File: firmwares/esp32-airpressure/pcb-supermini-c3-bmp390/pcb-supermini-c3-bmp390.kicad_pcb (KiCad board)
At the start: 2 copper layers, 43.8 x 70.8 mm, 11 parts, among them J1 JST GH 4_Socket, U1 ESP32-C3_SUPERMINI_SMD, U2 BMP390 MODULE, U3 CAN transciever

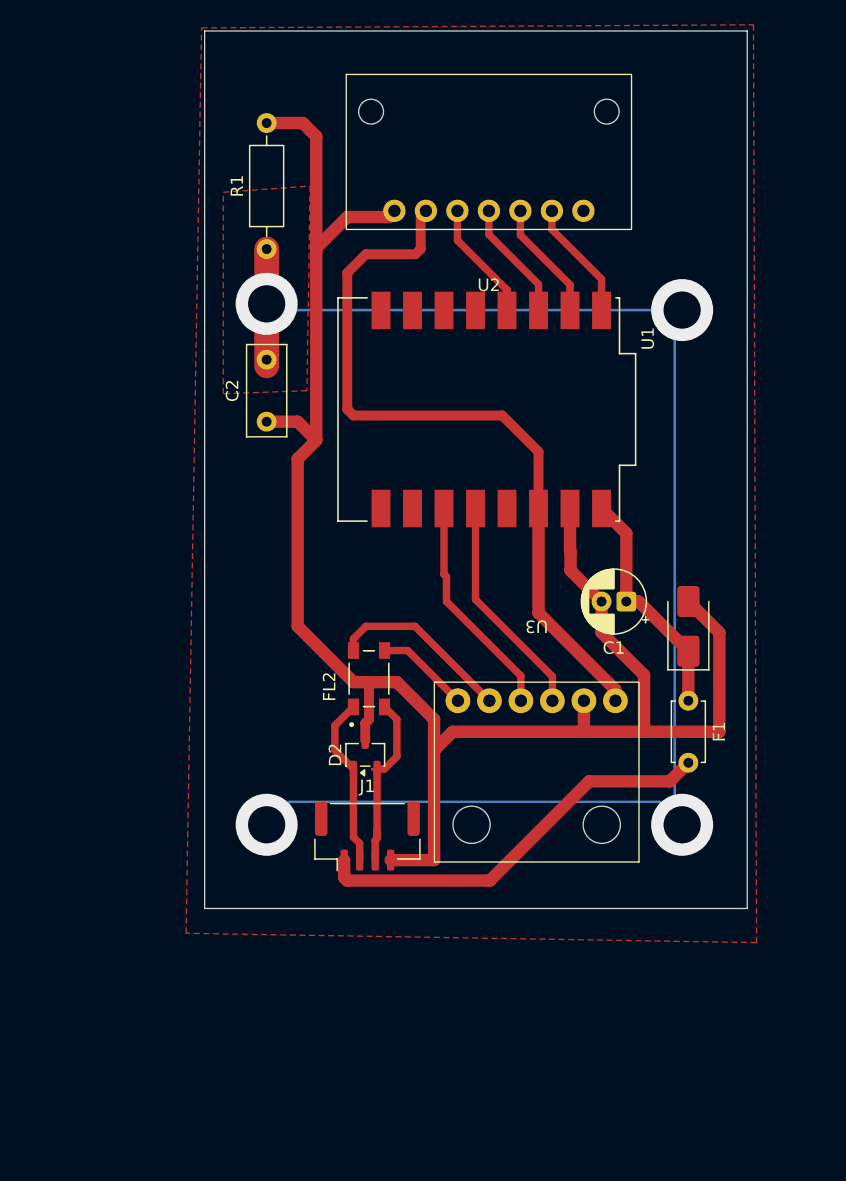
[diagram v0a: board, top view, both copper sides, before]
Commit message: refactor: update PCB to be on 2 layers
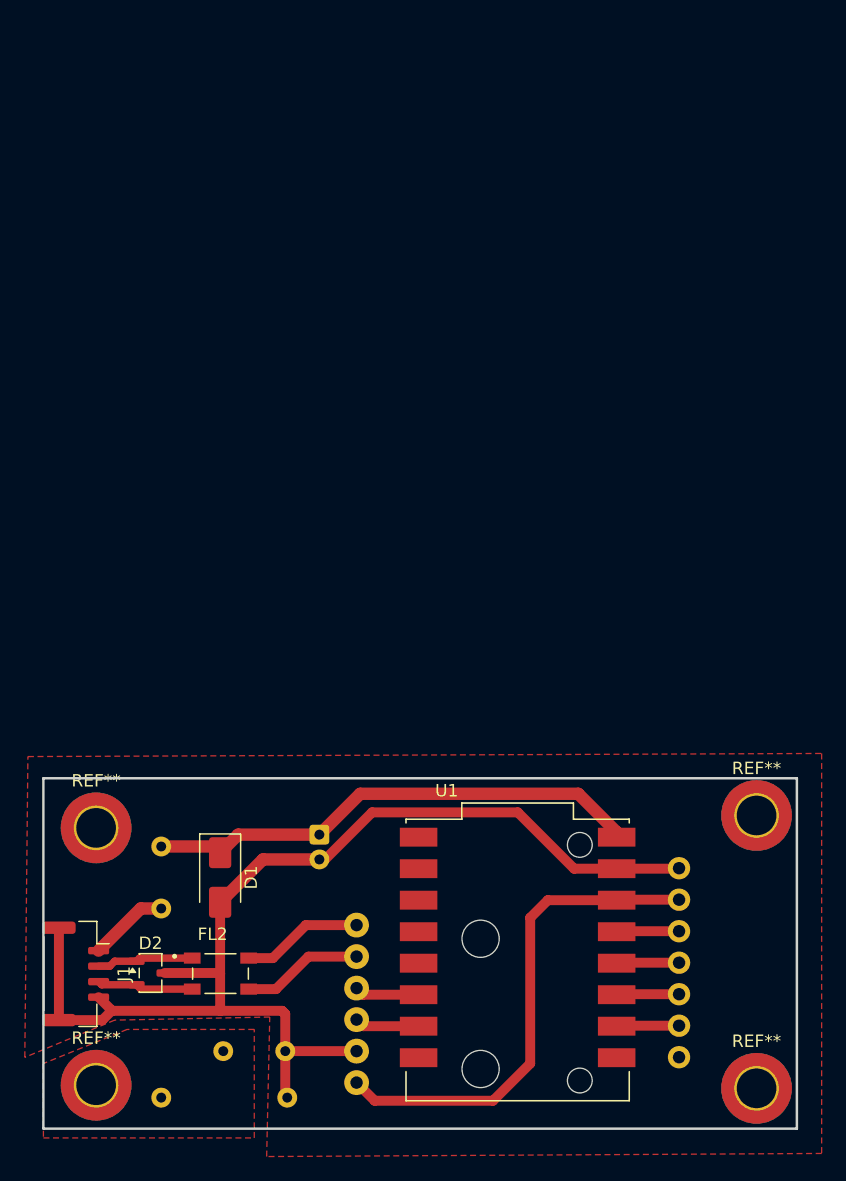
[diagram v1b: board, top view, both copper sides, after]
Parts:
- added REF**: MountingHole_3.2mm_M3_ISO7380_Pad_TopBottom, MountingHole:MountingHole_3.2mm_M3_ISO7380_Pad_TopBottom, F.Cu at (138.0, 141.2)
- added REF**: MountingHole_3.2mm_M3_ISO7380_Pad_TopBottom, MountingHole:MountingHole_3.2mm_M3_ISO7380_Pad_TopBottom, F.Cu at (84.8, 141.0)
- added REF**: MountingHole_3.2mm_M3_ISO7380_Pad_TopBottom, MountingHole:MountingHole_3.2mm_M3_ISO7380_Pad_TopBottom, F.Cu at (84.8, 120.2)
- added REF**: MountingHole_3.2mm_M3_ISO7380_Pad_TopBottom, MountingHole:MountingHole_3.2mm_M3_ISO7380_Pad_TopBottom, F.Cu at (138.0, 119.2)
- C1, C2, F1, R1, U2, U3: moved to B.Cu
- J1: footprint Connector_JST:JST_GH_BM04B-GHS-TBT_1x04-1MP_P1.25mm_Vertical -> Connector_JST:JST_GH_SM04B-GHS-TB_1x04-1MP_P1.25mm_Horizontal
- moved R1 68.9 mm to (90.0, 142.0), turned to 0 degrees
- moved U2 61.5 mm to (133.2, 131.1), turned to -90 degrees
- moved C2 50.8 mm to (100.0, 138.2), turned to 180 degrees
- moved U1 44.5 mm to (118.7, 130.9), turned to 0 degrees
- moved F1 44.1 mm to (90.0, 121.8)
- moved D1 42.8 mm to (94.8, 124.2), turned to -90 degrees
- moved C1 31.1 mm to (102.8, 120.8), turned to -90 degrees
- moved U3 30.5 mm to (104.2, 134.4), turned to 90 degrees
- moved FL2 26.6 mm to (94.8, 132.0), turned to 0 degrees
- moved J1 26.0 mm to (83.1, 132.0), turned to -90 degrees
- moved D2 24.7 mm to (89.1, 131.9), turned to 0 degrees
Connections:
- net GND renamed GND-EMS
- FL2 pad 3: Net-(U3-CANL) -> Net-(U3-CANH)
- FL2 pad 4: Net-(U3-CANH) -> Net-(U3-CANL)
- U1 pad 1: unconnected-(U1-GPIO1-Pad1) -> Net-(U1-GPIO1)
- U1 pad 10: unconnected-(U1-GPIO10-Pad10) -> Net-(U1-GPIO10)
- U1 pad 20: unconnected-(U1-GPIO20-Pad20) -> Net-(U1-GPIO20)
- U1 pad 4: unconnected-(U1-GPIO4-Pad4) -> Net-(U1-GPIO4)
- U1 pad 5: Net-(U1-GPIO5) -> unconnected-(U1-GPIO5-Pad5)
- U1 pad 6: Net-(U1-GPIO6) -> unconnected-(U1-GPIO6-Pad6)
- U1 pad 7: Net-(U1-GPIO7) -> unconnected-(U1-GPIO7-Pad7)
- U1 pad 8: Net-(U1-GPIO8) -> unconnected-(U1-GPIO8-Pad8)
- U2 pad 3: Net-(U1-GPIO8) -> Net-(U1-GPIO4)
- U2 pad 4: Net-(U1-GPIO7) -> Net-(U1-GPIO3)
- U2 pad 5: Net-(U1-GPIO6) -> Net-(U1-GPIO2)
- U2 pad 6: Net-(U1-GPIO5) -> Net-(U1-GPIO1)
- U3 pad 3: Net-(U1-GPIO3) -> Net-(U1-GPIO20)
- U3 pad 4: Net-(U1-GPIO2) -> Net-(U1-GPIO10)
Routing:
- net GND-EMS: track 120.2 -> 0.00 mm, vias 4 -> 0
- net GNDREF: track 148.8 -> 95.4 mm
- net VCC: track 33.2 -> 6.46 mm
- net Net-(D1-A1): track 19.0 -> 40.6 mm
- net Net-(U1-3V3): track 59.8 -> 40.2 mm
- net Net-(U1-GPIO3): track 18.1 -> 5.05 mm
- net Net-(U1-GPIO2): track 18.1 -> 5.05 mm
- net Net-(U1-GPIO8): track 9.69 -> 0.00 mm
- net Net-(U1-GPIO7): track 9.69 -> 0.00 mm
- net Net-(U1-GPIO6): track 9.69 -> 0.00 mm
- net Net-(U1-GPIO5): track 9.69 -> 0.00 mm
- net CAN_L: track 14.6 -> 7.80 mm
- net CAN_H: track 13.8 -> 7.82 mm
- net Net-(U1-GPIO20): track 0.00 -> 5.22 mm
- net Net-(U1-GPIO10): track 0.00 -> 5.22 mm
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- added copper zone on F.Cu, net GND-EMS
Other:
- board size 43.8 x 70.8 mm -> 60.8 x 28.2 mm

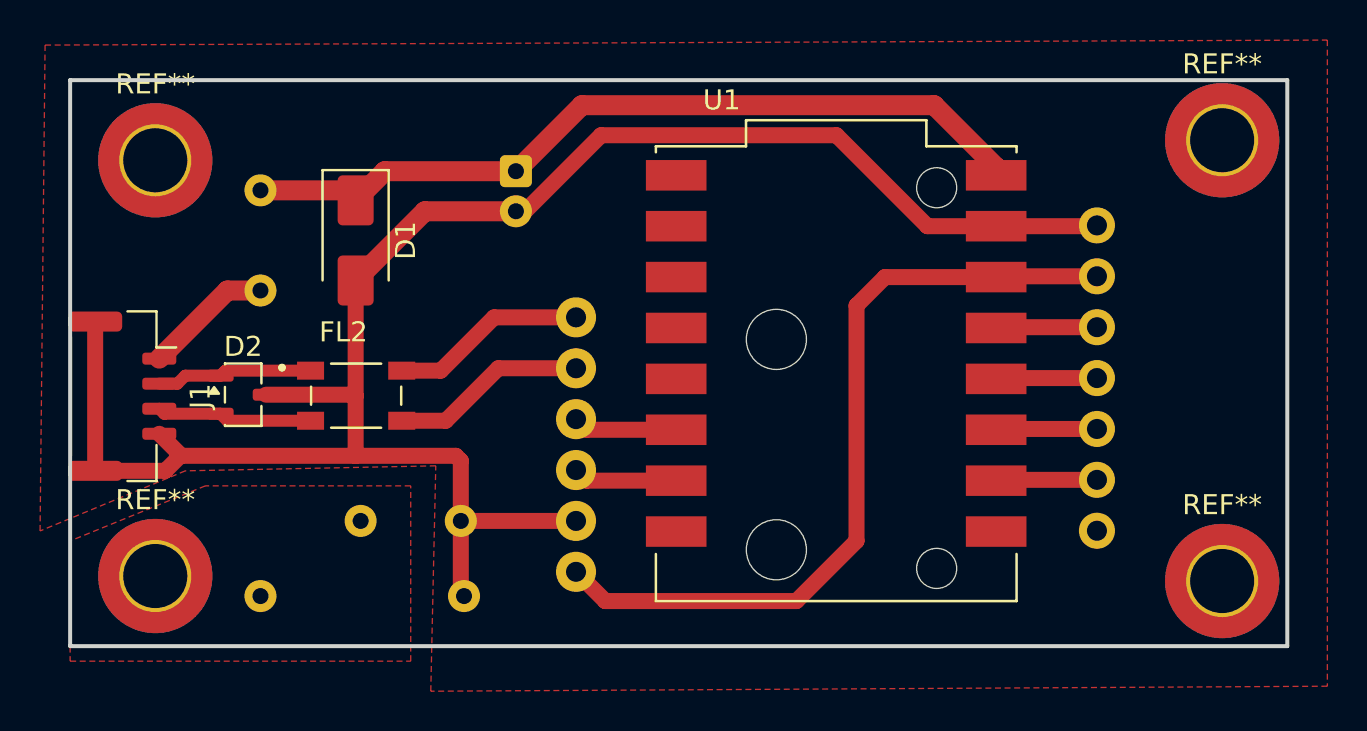
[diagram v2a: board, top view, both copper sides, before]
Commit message: Refactor ESP32 Gateway Firmware
- Updated main.c to include cannelloni_bridge and improved task management.
- Modified project_config.h to change CAN TX/RX pins and added Cannelloni configuration parameters.
- Added new HTML files for station mode configuration, device status, and system settings.
- Created a template HTML file for consistent UI styling across the web interface.
- Enhanced wifi_manager.c to improve WiFi connection handling and added support for Cannelloni services.
- Updated sdkconfig to set the CPU frequency to 240 MHz for better performance.
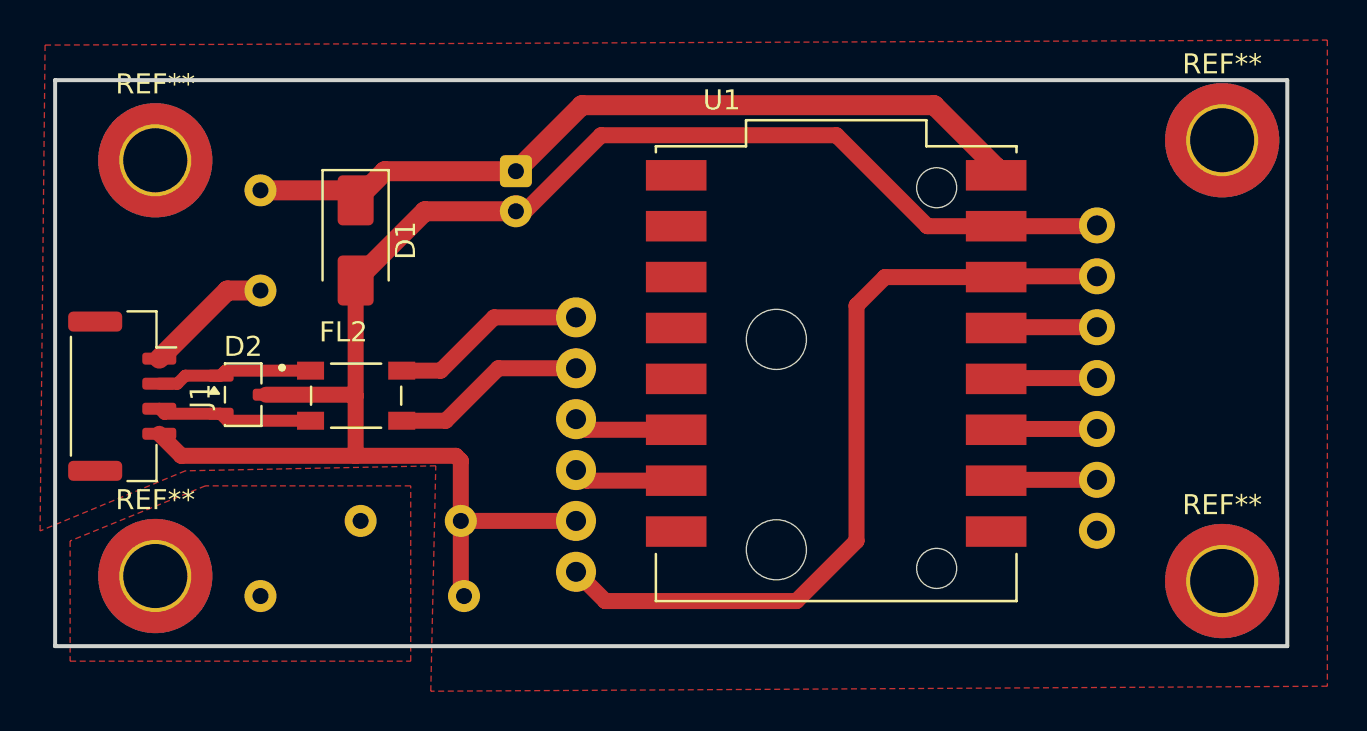
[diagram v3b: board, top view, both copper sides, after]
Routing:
- net GNDREF: track 95.4 -> 83.3 mm
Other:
- board size 60.8 x 28.2 mm -> 61.5 x 28.2 mm
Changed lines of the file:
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@@
 	)
 	(gr_rect
-		(start 80.5 116.25)
+		(start 79.75 116.25)
 		(end 141.25 144.5)
 		(stroke
@@
 	)
 	(segment
-		(start 85.25 135.75)
-		(end 86.025 134.975)
-		(width 0.8)
-		(layer "F.Cu")
-		(net "GNDREF")
-	)
-	(segment
 		(start 100 135.25)
 		(end 100 138.25)
@@
 		(end 98.205112 122.794888)
 		(width 1)
-		(layer "F.Cu")
-		(net "GNDREF")
-	)
-	(segment
-		(start 81.75 128.3)
-		(end 81.75 135.75)
-		(width 0.8)
 		(layer "F.Cu")
 		(net "GNDREF")
@@
 		(width 0.8)
 		(layer "F.Cu")
-		(net "GNDREF")
-	)
-	(segment
-		(start 81.75 135.75)
-		(end 85.25 135.75)
-		(width 0.8)
-		(layer "F.Cu")
